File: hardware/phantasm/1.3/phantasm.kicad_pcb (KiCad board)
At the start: 4 copper layers, 58.3 x 32 mm, 34 parts, among them J1 TBC05-02-1-G-G +5V IN ~1A, J2 TBC05-03-1-G-G LED DI/SIG_GND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, J3A TBC05-04-1-G-G SYNC in, J3B TBC05-04-1-G-G SYNC out, U1 74AHCT125

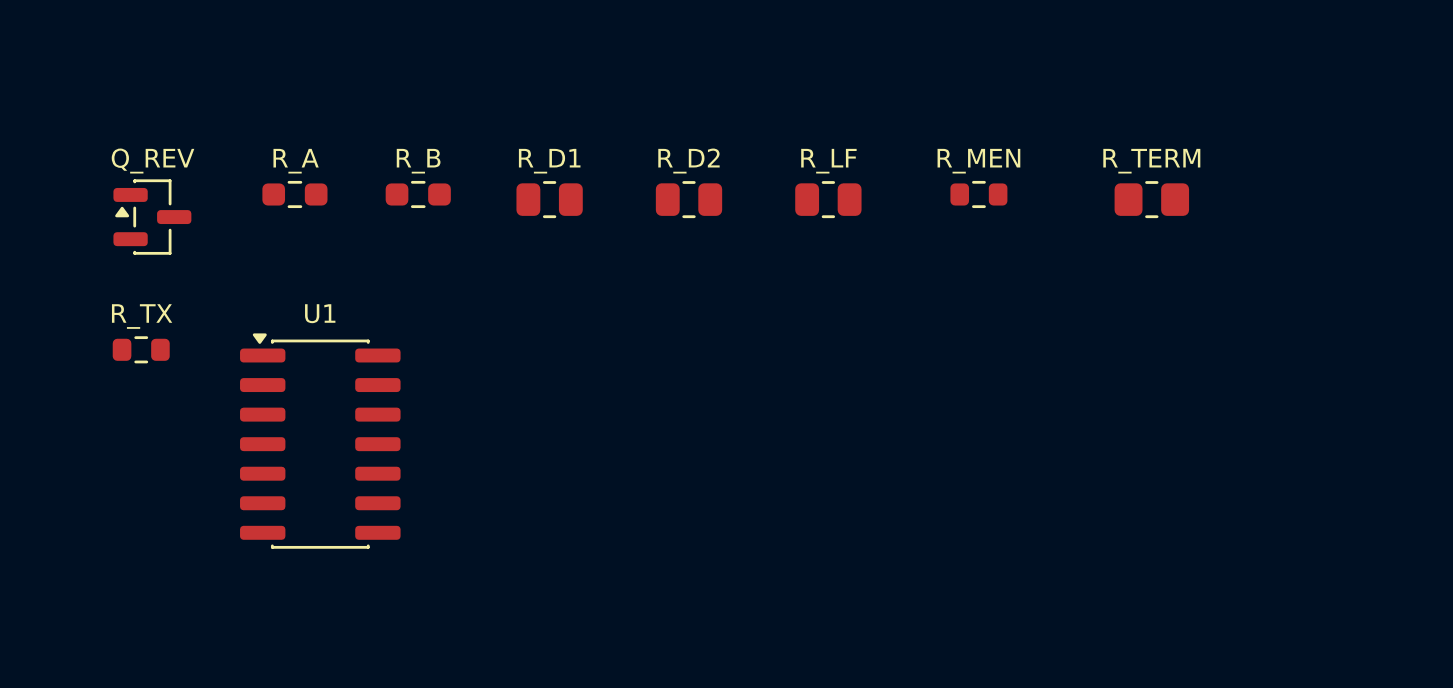
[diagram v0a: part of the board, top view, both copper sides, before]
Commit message: pcb: strengthen rev 1.3 differential sync and specify components
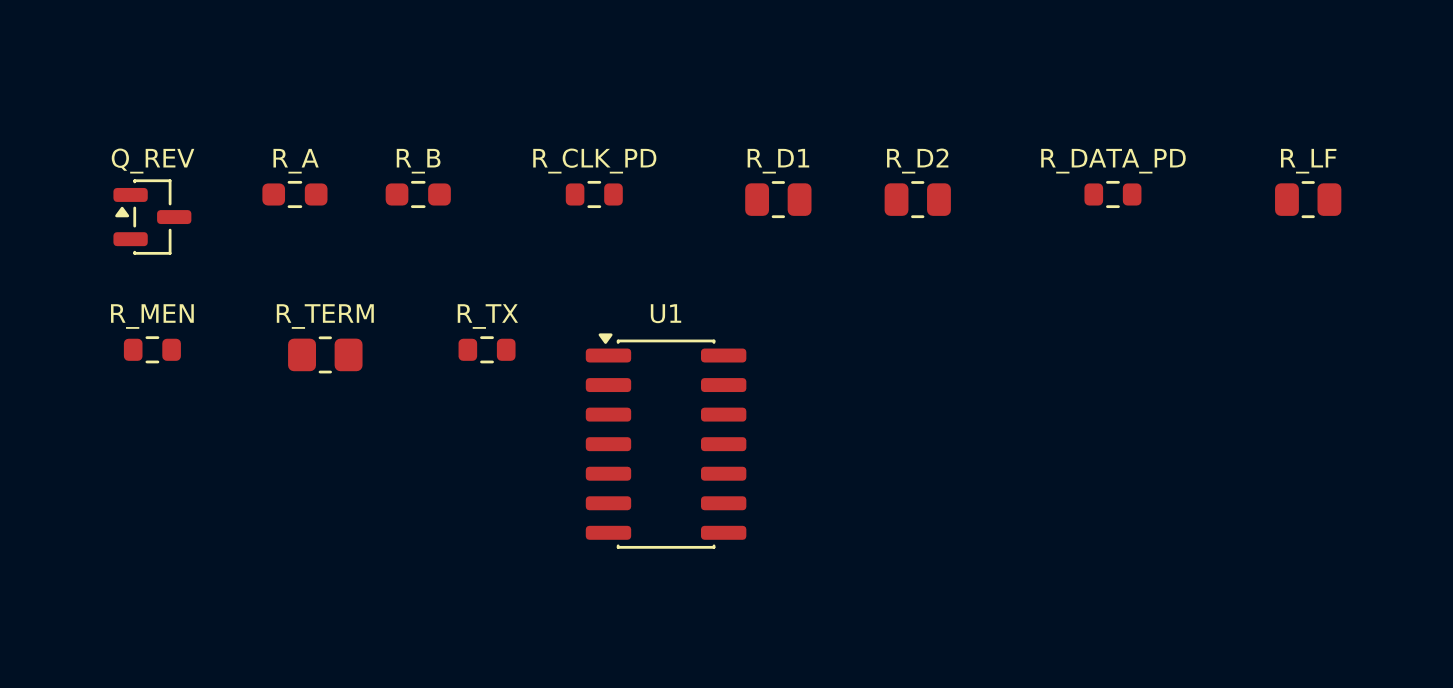
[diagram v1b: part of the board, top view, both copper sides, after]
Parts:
- added H3: M2.5, MountingHole:MountingHole_2.7mm_M2.5, F.Cu at (54.8, 3.50)
- added H4: M2.5, MountingHole:MountingHole_2.7mm_M2.5, F.Cu at (54.8, 28.5)
- C_BULK3: renamed from R_B; value 10R CRCW0603010RJNEAHP -> 1uF; footprint Resistor_SMD:R_0603_1608Metric_Pad0.98x0.95mm_HandSolder -> Capacitor_SMD:C_0603_1608Metric
- C_DEC2: renamed from U_SYNC; value THVD1410DR -> 0.1uF; footprint Package_SO:SOIC-8_3.9x4.9mm_P1.27mm -> Capacitor_SMD:C_0603_1608Metric
- C_DEC3: renamed from R_A; value 10R CRCW0603010RJNEAHP -> 0.1uF; footprint Resistor_SMD:R_0603_1608Metric_Pad0.98x0.95mm_HandSolder -> Capacitor_SMD:C_0603_1608Metric
- D_SYNC: renamed from J3B; value TBC05-04-1-G-G SYNC out -> CDSOT23-SM712; footprint phantasm:TerminalBlock_GCT_TBC05-04-1-G-G -> Package_TO_SOT_SMD:SOT-23
- J2: renamed from C_DEC3; value 0.1uF -> TBC05-03-1-G-G LED DI/SIG_GND/CI; footprint Capacitor_SMD:C_0603_1608Metric -> phantasm:TerminalBlock_GCT_TBC05-03-1-G-G
- J3A: renamed from R_TERM; value 120R 1% 0.25W -> TBC05-04-1-G-G SYNC in; footprint Resistor_SMD:R_0805_2012Metric_Pad1.20x1.40mm_HandSolder -> phantasm:TerminalBlock_GCT_TBC05-04-1-G-G
- J3B: renamed from JP_TERM; value TERM endpoints only -> TBC05-04-1-G-G SYNC out; footprint Jumper:SolderJumper-2_P1.3mm_Open_RoundedPad1.0x1.5mm -> phantasm:TerminalBlock_GCT_TBC05-04-1-G-G
- JP_ID0: renamed from JP_ID2; value ID2->GND (N=8) -> ID0->GND
- JP_ID1: renamed from H1; value M2.5 -> ID1->GND; footprint MountingHole:MountingHole_2.7mm_M2.5 -> Jumper:SolderJumper-2_P1.3mm_Open_RoundedPad1.0x1.5mm
- JP_ID2: renamed from H2; value M2.5 -> ID2->GND (N=8); footprint MountingHole:MountingHole_2.7mm_M2.5 -> Jumper:SolderJumper-2_P1.3mm_Open_RoundedPad1.0x1.5mm
- JP_SHLD: renamed from JP_ID0; value ID0->GND -> shield gnd (master only)
- JP_TERM: renamed from R_MEN; value 10k -> TERM endpoints only; footprint Resistor_SMD:R_0603_1608Metric -> Jumper:SolderJumper-2_P1.3mm_Open_RoundedPad1.0x1.5mm
- R_A: renamed from D_SYNC; value CDSOT23-SM712 -> 10R 1% pulse-proof; footprint Package_TO_SOT_SMD:SOT-23 -> Resistor_SMD:R_0603_1608Metric_Pad0.98x0.95mm_HandSolder
- R_B: renamed from J3A; value TBC05-04-1-G-G SYNC in -> 10R 1% pulse-proof; footprint phantasm:TerminalBlock_GCT_TBC05-04-1-G-G -> Resistor_SMD:R_0603_1608Metric_Pad0.98x0.95mm_HandSolder
- R_CLK_PD: renamed from C_DEC2; value 0.1uF -> 10k; footprint Capacitor_SMD:C_0603_1608Metric -> Resistor_SMD:R_0603_1608Metric
- R_MEN: renamed from JP_ID1; value ID1->GND -> 10k; footprint Jumper:SolderJumper-2_P1.3mm_Open_RoundedPad1.0x1.5mm -> Resistor_SMD:R_0603_1608Metric
- R_TERM: renamed from JP_SHLD; value shield gnd (master only) -> 120R 1% 0.5W; footprint Jumper:SolderJumper-2_P1.3mm_Open_RoundedPad1.0x1.5mm -> Resistor_SMD:R_0805_2012Metric_Pad1.20x1.40mm_HandSolder
- R_TX: renamed from J2; value TBC05-03-1-G-G LED DI/SIG_GND/CI -> 10k; footprint phantasm:TerminalBlock_GCT_TBC05-03-1-G-G -> Resistor_SMD:R_0603_1608Metric
- U_SYNC: renamed from C_BULK3; value 1uF -> THVD2410DR; footprint Capacitor_SMD:C_0603_1608Metric -> Package_SO:SOIC-8_3.9x4.9mm_P1.27mm
- moved R_MEN 89.9 mm to (4.47, 85.6), turned to 0 degrees
- moved C_DEC2 84.4 mm to (21.7, 40.0)
- moved U_SYNC 82.8 mm to (5.70, 122.8)
- moved R_B 81.5 mm to (15.9, 78.9)
- moved R_TERM 80.0 mm to (11.9, 85.8), turned to 0 degrees
- moved J3A 75.2 mm to (48.0, 3.96)
- moved R_TX 64.1 mm to (18.9, 85.6)
- moved D_SYNC 56.3 mm to (4.96, 52.8)
- moved JP_ID2 54.1 mm to (56.0, 15.3), turned to 90 degrees
- moved JP_ID1 53.2 mm to (56.0, 11.9), turned to 90 degrees
- moved H1 51.3 mm to (3.50, 3.50)
- moved H2 51.3 mm to (3.50, 28.5)
- moved J3B 49.3 mm to (48.0, 16.5)
- moved C_DEC3 43.3 mm to (29.6, 40.0)
- moved R_DATA_PD 42.3 mm to (45.8, 78.9)
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- renumbered H3 to H1, H4 to H2, R_TX to R_DATA_PD
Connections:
- C_BULK3 pad 1: /SYNC_B -> +3V3
- C_BULK3 pad 2: /SYNC_B_IC -> GND
- C_DEC2 pad 1: /FRAME_SYNC -> +5V_LOGIC
- C_DEC3 pad 1: /SYNC_A -> +3V3
- C_DEC3 pad 2: /SYNC_A_IC -> GND
- J2 pad 1: +3V3 -> /DATA
- J3A pad 2: /TERM_LINK -> /SYNC_B
- J3B pad 1: /TERM_LINK -> /SYNC_A
- JP_ID0 pad 1: /ID2 -> /ID0
- JP_SHLD pad 1: /ID0 -> /SHIELD
- JP_TERM pad 1: GND -> /TERM_LINK
- JP_TERM pad 2: /MASTER_EN -> /SYNC_B
- R_A pad 2: /SYNC_B -> /SYNC_A_IC
- R_B pad 1: /SYNC_A -> /SYNC_B
- R_B pad 2: /SYNC_B -> /SYNC_B_IC
- R_CLK_PD pad 1: +5V_LOGIC -> /CLK_IN
- R_DATA_PD pad 1: /SYNC_TX -> /DATA_IN
- R_DATA_PD pad 2: +3V3 -> GND
- R_MEN pad 1: /ID1 -> GND
- R_MEN pad 2: GND -> /MASTER_EN
- R_TERM pad 1: /SHIELD -> /SYNC_A
- R_TERM pad 2: GND -> /TERM_LINK
- R_TX pad 1: /DATA -> /SYNC_TX
- R_TX pad 2: GND -> +3V3
- U_SYNC pad 1: +3V3 -> /FRAME_SYNC
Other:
- board text removed: "BOARD ID: ____"
